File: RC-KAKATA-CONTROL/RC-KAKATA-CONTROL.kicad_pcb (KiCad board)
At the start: 4 copper layers, 160 x 160 mm, 172 parts, among them J1 Conn_02x20_Socket_DG250T-5.0-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, J10 DB125-2.54-4P-GN, J11 Screw_Terminal_01x02, J12 Conn_01x07, J13 Screw_Terminal_01x02, J17 Screw_Terminal_01x02, J19 Screw_Terminal_01x02, J2 Screw_Terminal_01x02, J21 Screw_Terminal_01x02, J23 Screw_Terminal_01x02, J25 Conn_02x20_Socket_DG250T-5.0-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, J3 Screw_Terminal_01x02, J4 Screw_Terminal_01x02, J5 Screw_Terminal_01x02, J6 Raspberry_Pi_2x20_PTH, J7 Screw_Terminal_01x02, J8 DB125-2.54-4P-GN, J9 Screw_Terminal_01x02, SW1 TS-1088-AR02016, SW2 TS-1088-AR02016, SW3 TS-1088-AR02016, SW4 TS-1088-AR02016, SW6 TS-1088-AR02016, U1 PS-TO220, U13 ICM-20689, U2 PS-TO220, U3 STM32H743IIT6, U4 YK16S-L7.2-B10KA(32-8)-G-A29, U8 W25Q128JVSIQTR, X1 SMD3225-4, X2 Q13MC3061000300

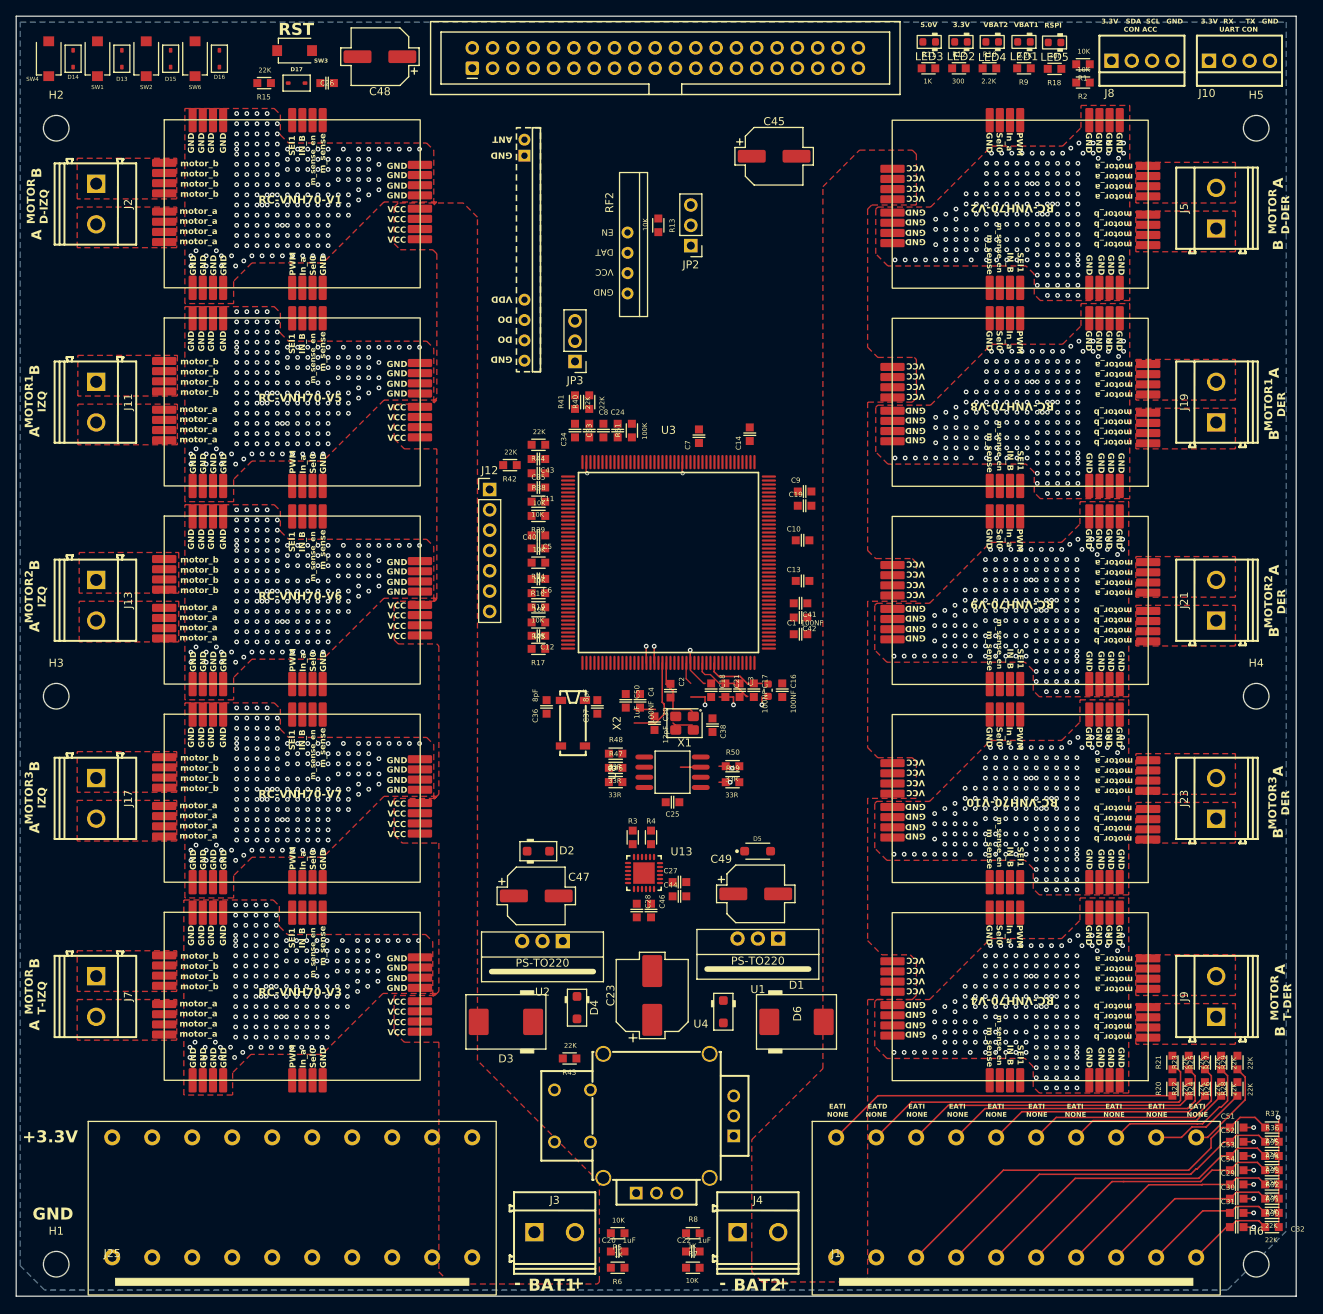
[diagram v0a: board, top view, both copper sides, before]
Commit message: Creadas Conexiones de GND y +3.3V Creada Conexion de +5 Creadas las conexiones criticas de Flash - SPI - I2C
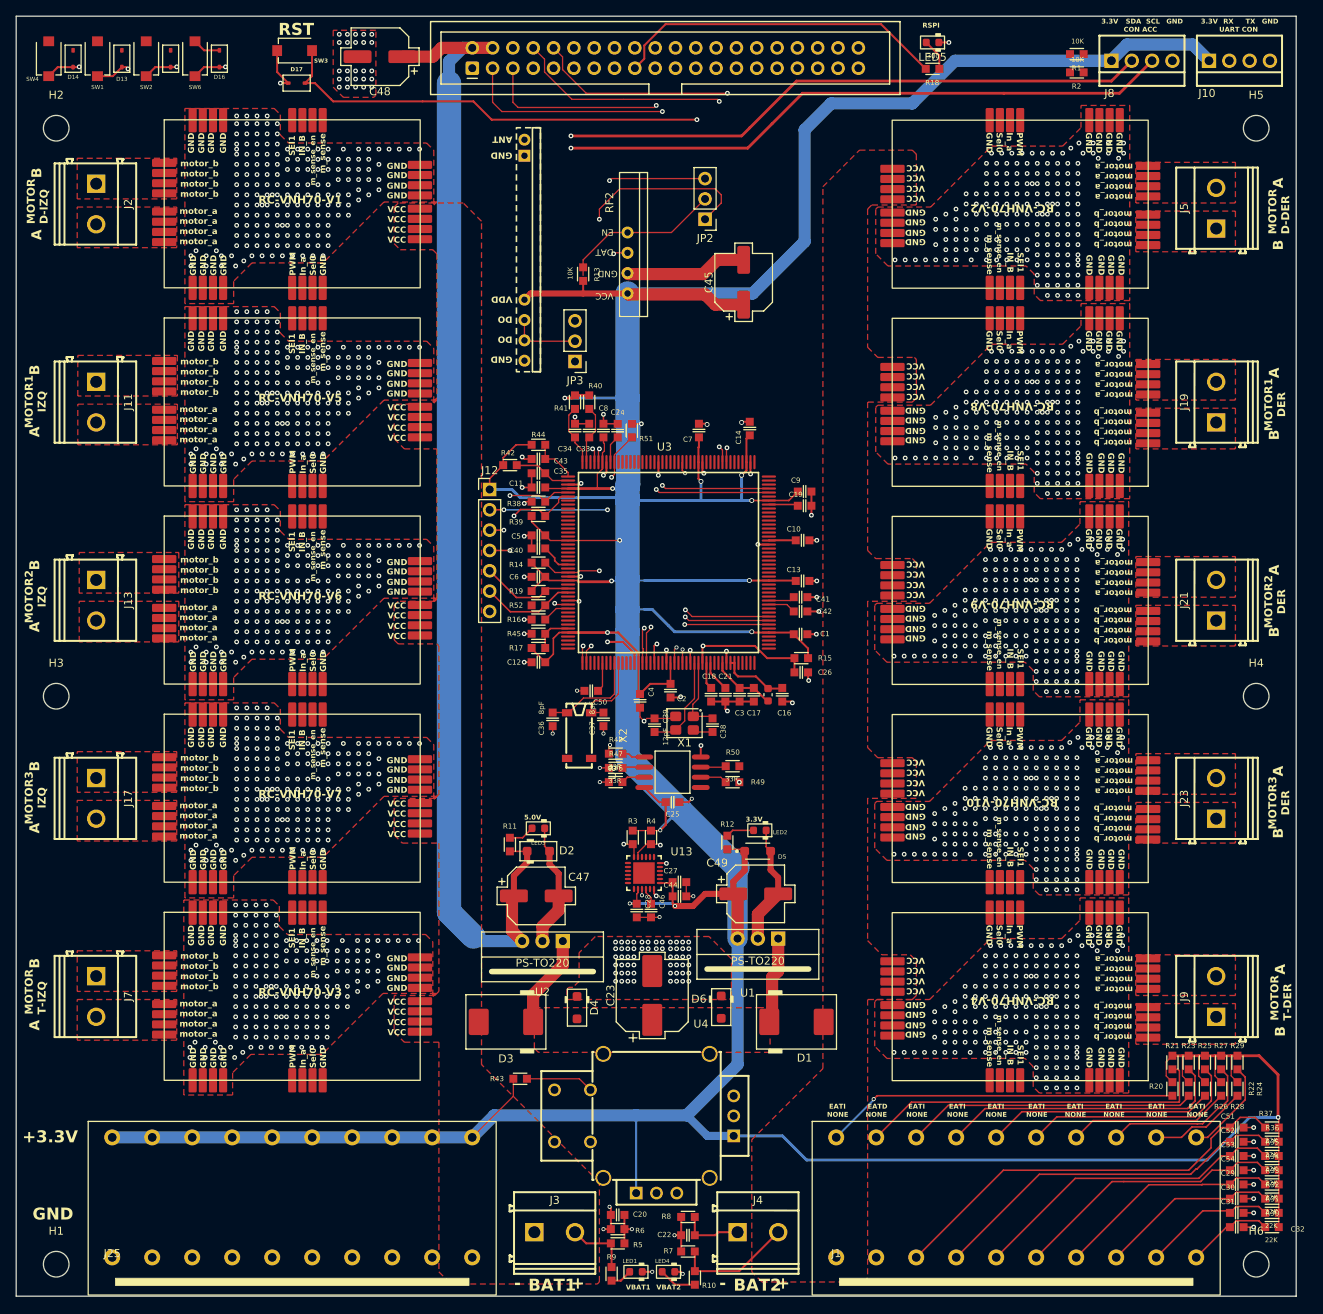
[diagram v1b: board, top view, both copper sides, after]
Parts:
- added R52: 10K, 4ms_Resistor:R_0603, F.Cu at (159.8, 131.6)
- moved LED1 161.2 mm to (172.0, 215.0)
- moved R9 159.3 mm to (168.9, 215.2), turned to -90 degrees
- moved LED4 159.0 mm to (176.0, 215.0)
- moved R10 155.6 mm to (179.3, 215.7), turned to -90 degrees
- moved R11 110.2 mm to (156.2, 161.5), turned to 90 degrees
- moved LED3 109.8 mm to (159.8, 159.5)
- moved LED2 101.7 mm to (187.5, 159.8)
- moved R12 101.0 mm to (183.4, 161.3), turned to 90 degrees
- moved R15 98.4 mm to (192.6, 138.2), turned to 180 degrees
- moved C26 94.5 mm to (192.6, 140.0)
- moved C45 16.2 mm to (185.4, 91.3), turned to 90 degrees
- moved LED5 15.3 mm to (209.0, 61.3)
- moved R18 15.3 mm to (209.0, 64.6)
- moved R13 11.2 mm to (165.4, 90.2)
- moved R43 6.69 mm to (157.5, 190.8)
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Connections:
- net Net-(D1-K) renamed /power_supply/vbat_in
- J12 pad 5: /NJTRST -> /JTDO
- J12 pad 6: /JTDO -> /NJTRST
- J6 pad 11: /RPI_GPIO_17 -> unconnected-(J6-GPIO17-Pad11)
- J6 pad 12: /RPI_GPIO_18 -> unconnected-(J6-GPIO18/PWM0-Pad12)
- J6 pad 36: /RPI_GPIO_16 -> unconnected-(J6-GPIO16-Pad36)
- R19 pad 2: /NJTRST -> /JTDO
- U3 pad 119: /RPI_GPIO_16 -> unconnected-(U3-PA8-Pad119)
- U3 pad 120: /RPI_GPIO_17 -> unconnected-(U3-PA9-Pad120)
- U3 pad 121: /RPI_GPIO_18 -> unconnected-(U3-PA10-Pad121)
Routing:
- net +3.3V: track 21.8 -> 723.6 mm, vias 1 -> 15
- net GND: track 21.8 -> 174.4 mm, vias 1751 -> 1879
- net +5V: track 0.00 -> 147.0 mm
- net /nrst: track 0.00 -> 137.7 mm, vias 0 -> 2
- net /ACC_I2C_SCL: track 0.00 -> 137.3 mm, vias 0 -> 2
- net /ACC_I2C_SDA: track 0.00 -> 135.4 mm, vias 0 -> 2
- net /RPI_GPIO_SDA: track 0.00 -> 86.3 mm, vias 0 -> 2
- net /RPI_GPIO_SCL: track 0.00 -> 85.4 mm, vias 0 -> 2
- net /RPI_SPI_CLK: track 0.00 -> 82.7 mm, vias 0 -> 1
- net /RPI_SPI_MOSI: track 0.00 -> 80.8 mm, vias 0 -> 1
- net /RPI_SPI_MISO: track 0.00 -> 80.1 mm, vias 0 -> 1
- net /RF_DATA_TIMER: track 0.00 -> 74.0 mm, vias 0 -> 2
- net /RPI_UART2_TX: track 0.00 -> 72.2 mm, vias 0 -> 2
- net /RPI_UART2_RX: track 0.00 -> 71.2 mm, vias 0 -> 2
- net /RF_DATA_UART_TX: track 0.00 -> 52.5 mm, vias 0 -> 2
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- added copper zone on F.Cu, net /power_supply/vbat_in
- added copper zone on In1.Cu, net GND
- removed copper zone on B.Cu, net GND

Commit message: Restan 32 pistas por rutear Colocados los Ref de los compoentes
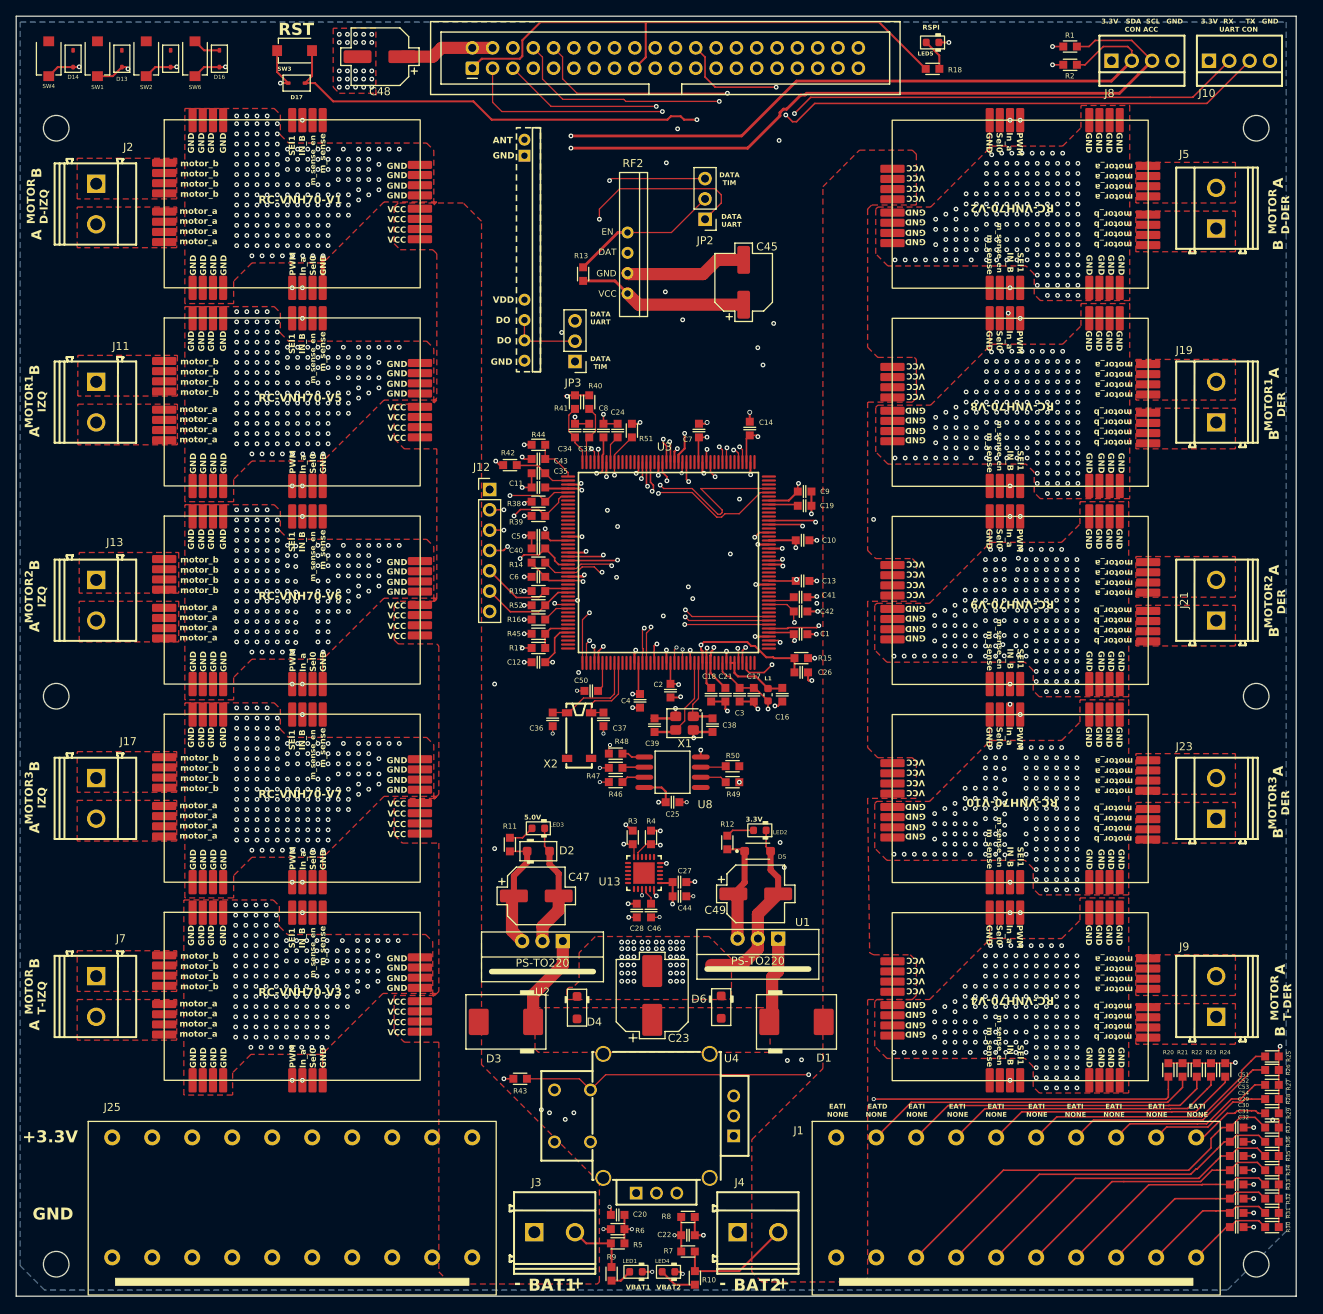
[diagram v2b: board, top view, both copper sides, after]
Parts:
- moved R25 8.42 mm to (251.5, 188.0), turned to 180 degrees
- moved R29 7.68 mm to (251.5, 195.1), turned to 180 degrees
- moved R27 6.94 mm to (251.5, 191.6), turned to 180 degrees
- moved R26 6.78 mm to (251.5, 189.7), turned to 180 degrees
- moved R28 4.50 mm to (251.5, 193.4), turned to 180 degrees
- moved R24 3.48 mm to (245.6, 189.7)
- moved R23 2.94 mm to (243.9, 189.7)
- moved R22 2.58 mm to (242.1, 189.7)
- moved R20 2.43 mm to (238.5, 189.7)
- moved R21 1.57 mm to (240.3, 189.7)
- moved R2 1.27 mm to (226.2, 64.1)
- moved R1 1.27 mm to (226.2, 61.8)
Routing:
- net +3.3V: track 723.6 -> 166.4 mm, vias 15 -> 34
- net /DIR_A_MOTOR_DER: track 0.00 -> 158.1 mm, vias 0 -> 7
- net /DIR_B_MOTOR_IZQ: track 0.00 -> 155.8 mm, vias 0 -> 6
- net /DIR_A_MOTOR_IZQ: track 0.00 -> 141.0 mm, vias 0 -> 7
- net /PWM_TRASERO_IZQ: track 0.00 -> 137.3 mm, vias 0 -> 3
- net /DIR_A_TRASERO_IZQ: track 0.00 -> 126.0 mm, vias 0 -> 3
- net +5V: track 147.0 -> 27.7 mm
- net /DIR_B_MOTOR_DER: track 0.00 -> 114.8 mm, vias 0 -> 5
- net /UART_TX: track 0.00 -> 108.3 mm, vias 0 -> 2
- net /DIR_B_TRASERO_IZQ: track 0.00 -> 105.2 mm, vias 0 -> 3
- net /UART_RX: track 0.00 -> 104.3 mm, vias 0 -> 2
- net /DIR_B_TRASERO_DER: track 1.53 -> 104.7 mm, vias 1 -> 3
- net /JOY_DIRB: track 11.8 -> 106.8 mm, vias 0 -> 2
- net /PWM_DELANTERO_IZQ: track 0.00 -> 93.7 mm, vias 0 -> 3
- net /RPI_SPI_CS: track 0.00 -> 91.2 mm, vias 0 -> 2
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- added copper zone on In1.Cu, net +3.3V
- added copper zone on In1.Cu, net +5V
- added copper zone on B.Cu, net GND
- removed copper zone on In1.Cu, net GND
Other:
- copper layers 4 -> 6
- board text added: "DATA TIM"
- board text added: "DATA UART"

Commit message: Terminadas las conexiones Verificadas las conexiones
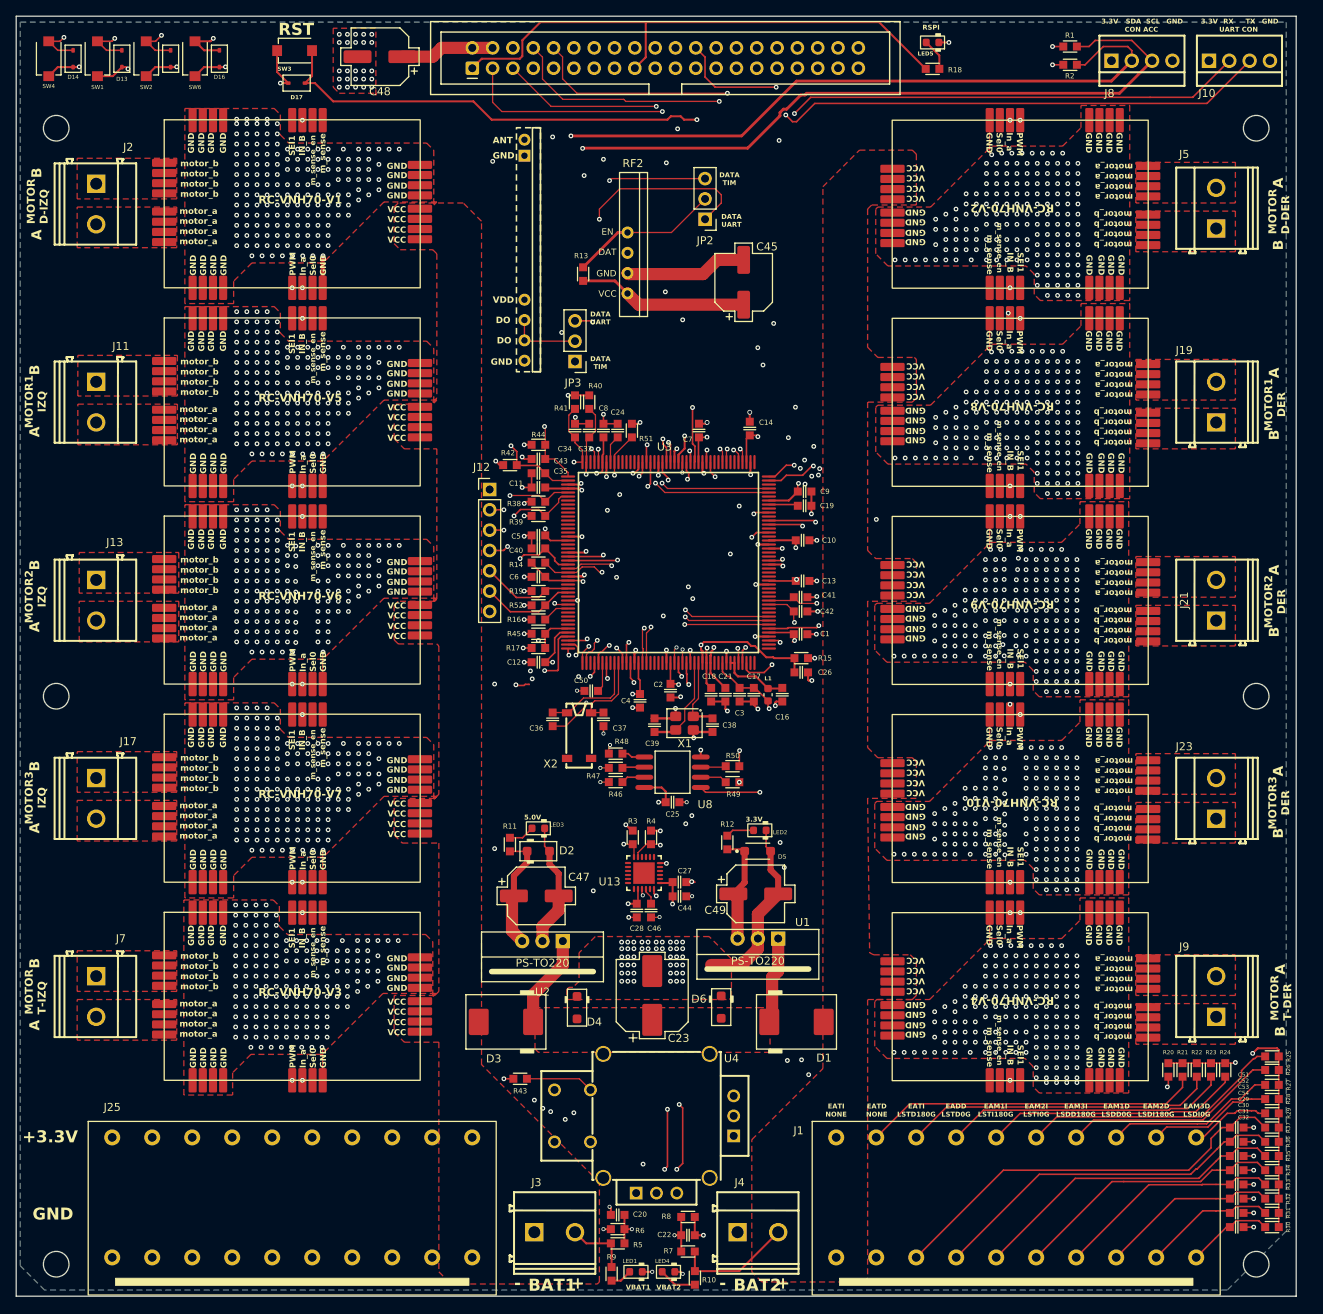
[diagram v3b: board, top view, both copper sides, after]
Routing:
- net /ENC_A_MOTOR_1_DER: track 21.3 -> 170.9 mm, vias 0 -> 3
- net /ENC_A_MOTOR_3_DER: track 10.1 -> 154.8 mm, vias 0 -> 2
- net /LS_TRASERO_IX_0G: track 34.0 -> 177.6 mm, vias 0 -> 3
- net /ENC_A_MOTOR_2_DER: track 15.6 -> 145.0 mm, vias 0 -> 1
- net /ENC_A_MOTOR_3_IZQ: track 28.7 -> 154.3 mm, vias 1 -> 2
- net /LS_TRASERO_IX_180G: track 39.7 -> 159.5 mm, vias 0 -> 2
- net /ENC_A_TRASERO_IZQ: track 50.2 -> 166.2 mm, vias 2 -> 3
- net /LS_TRASERO_DX_0G: track 45.3 -> 159.6 mm, vias 0 -> 4
- net /ENC_A_MOTOR_1_IZQ: track 34.3 -> 148.0 mm, vias 1 -> 2
- net /ENC_A_MOTOR_2_IZQ: track 33.3 -> 145.9 mm, vias 0 -> 1
- net /ENC_A_TRASERO_DER: track 45.3 -> 156.5 mm, vias 1 -> 2
- net /LS_TRASERO_DX_180G: track 52.1 -> 159.7 mm, vias 0 -> 4
- net /BUTON4: track 7.21 -> 114.6 mm, vias 0 -> 3
- net /BUTON3: track 5.84 -> 111.7 mm, vias 0 -> 3
- net /ENC_A_DELANTERO_IZQ: track 49.5 -> 155.0 mm, vias 1 -> 2
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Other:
- board text added: "EADD"
- board text added: "EAM1D"
- board text added: "EAM1I"
- board text added: "EAM2D"
- board text added: "EAM2I"
- board text added: "EAM3D"
- board text added: "EAM3I"
- board text added: "LSDD0G"
- board text added: "LSDD180G"
- board text added: "LSDI0G"
- board text added: "LSDI180G"
- board text added: "LSTD0G"
- board text added: "LSTD180G"
- board text added: "LSTI0G"
- board text added: "LSTI180G"

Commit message: Se verifico el PCB Los poligonos Los clereance
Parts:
- moved C5 0.15 mm to (159.8, 122.8)
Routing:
- net /FLASH_IO_1: track 21.0 -> 31.6 mm
- net GND: track 222.6 -> 220.5 mm
- net /ADC_VBAT1: track 95.9 -> 93.9 mm
- net /FLASH_IO_3: track 30.0 -> 31.8 mm
- net /LS_TRASERO_IX_0G: track 177.6 -> 175.8 mm
- net /ADC_VBAT2: track 93.1 -> 91.6 mm
- net /FLASH_CLK: track 30.4 -> 31.7 mm
- net /UART_TX: track 108.2 -> 107.3 mm
- net /BUTON3: track 111.7 -> 110.8 mm

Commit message: Completado el BOM
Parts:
- added J14: DB125-2.54-4P-GN, EasyEDA:CONN-TH_DB125-2.54-4P-GN, F.Cu at (217.8, 63.6)
- added R53: 10K, 4ms_Resistor:R_0603, F.Cu at (192.0, 77.0)
- added R54: 10K, 4ms_Resistor:R_0603, F.Cu at (192.0, 79.6)
- added R55: 10K, 4ms_Resistor:R_0603, F.Cu at (192.0, 82.1)
- added TP1: TestPoint_Hole1, 4ms_TestPoint:TestPoint_WireHole, B.Cu at (182.9, 130.2)
- added TP2: TestPoint_Hole1, 4ms_TestPoint:TestPoint_WireHole, B.Cu at (183.7, 127.4)
- added TP3: TestPoint_Hole1, 4ms_TestPoint:TestPoint_WireHole, B.Cu at (181.0, 126.3)
- added TP4: TestPoint_Hole1, 4ms_TestPoint:TestPoint_WireHole, B.Cu at (181.2, 123.3)
- added TP5: TestPoint_Hole1, 4ms_TestPoint:TestPoint_WireHole, B.Cu at (181.2, 120.3)
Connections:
- U3 pad 59: unconnected-(U3-PF11-Pad59) -> Net-(U3-PF11)
- U3 pad 60: unconnected-(U3-PF12-Pad60) -> Net-(U3-PF12)
- U3 pad 63: unconnected-(U3-PF13-Pad63) -> Net-(U3-PF13)
- U3 pad 64: unconnected-(U3-PF14-Pad64) -> Net-(U3-PF14)
- U3 pad 65: unconnected-(U3-PF15-Pad65) -> Net-(U3-PF15)
- U3 pad 94: unconnected-(U3-PB14-Pad94) -> /ACC_1
- U3 pad 98: unconnected-(U3-PD10-Pad98) -> /ACC_2
- U3 pad 99: unconnected-(U3-PD11-Pad99) -> /ACC_3
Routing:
- net /ACC_3: track 0.00 -> 83.6 mm, vias 0 -> 3
- net /ACC_2: track 0.00 -> 83.2 mm, vias 0 -> 3
- net /ACC_1: track 0.00 -> 81.2 mm, vias 0 -> 4
- net Net-(U3-PF15): track 0.00 -> 10.7 mm
- net Net-(U3-PF14): track 0.00 -> 9.89 mm
- net Net-(U3-PF13): track 0.00 -> 8.17 mm
- net Net-(U3-PF12): track 0.00 -> 5.96 mm
- net /RPI_SPI_CS: track 92.5 -> 98.4 mm
- net Net-(U3-PF11): track 0.00 -> 5.78 mm
- net +3.3V: track 171.2 -> 174.8 mm, vias 33 -> 36
- net /UART_RX: track 104.3 -> 105.9 mm
- net /ACC_I2C_SCL: track 147.5 -> 148.8 mm
- net /DIR_A_MOTOR_DER: track 155.8 -> 156.8 mm
- net /ACC_I2C_SDA: track 144.7 -> 145.4 mm
- net /PWM_MOTOR_2_DER: track 66.1 -> 66.7 mm
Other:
- board text added: "ACT1"
- board text added: "ACT2"
- board text added: "ACT3"
